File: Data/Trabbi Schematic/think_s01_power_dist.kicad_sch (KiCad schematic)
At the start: 3 parts, among them SW1 Ignition Switch

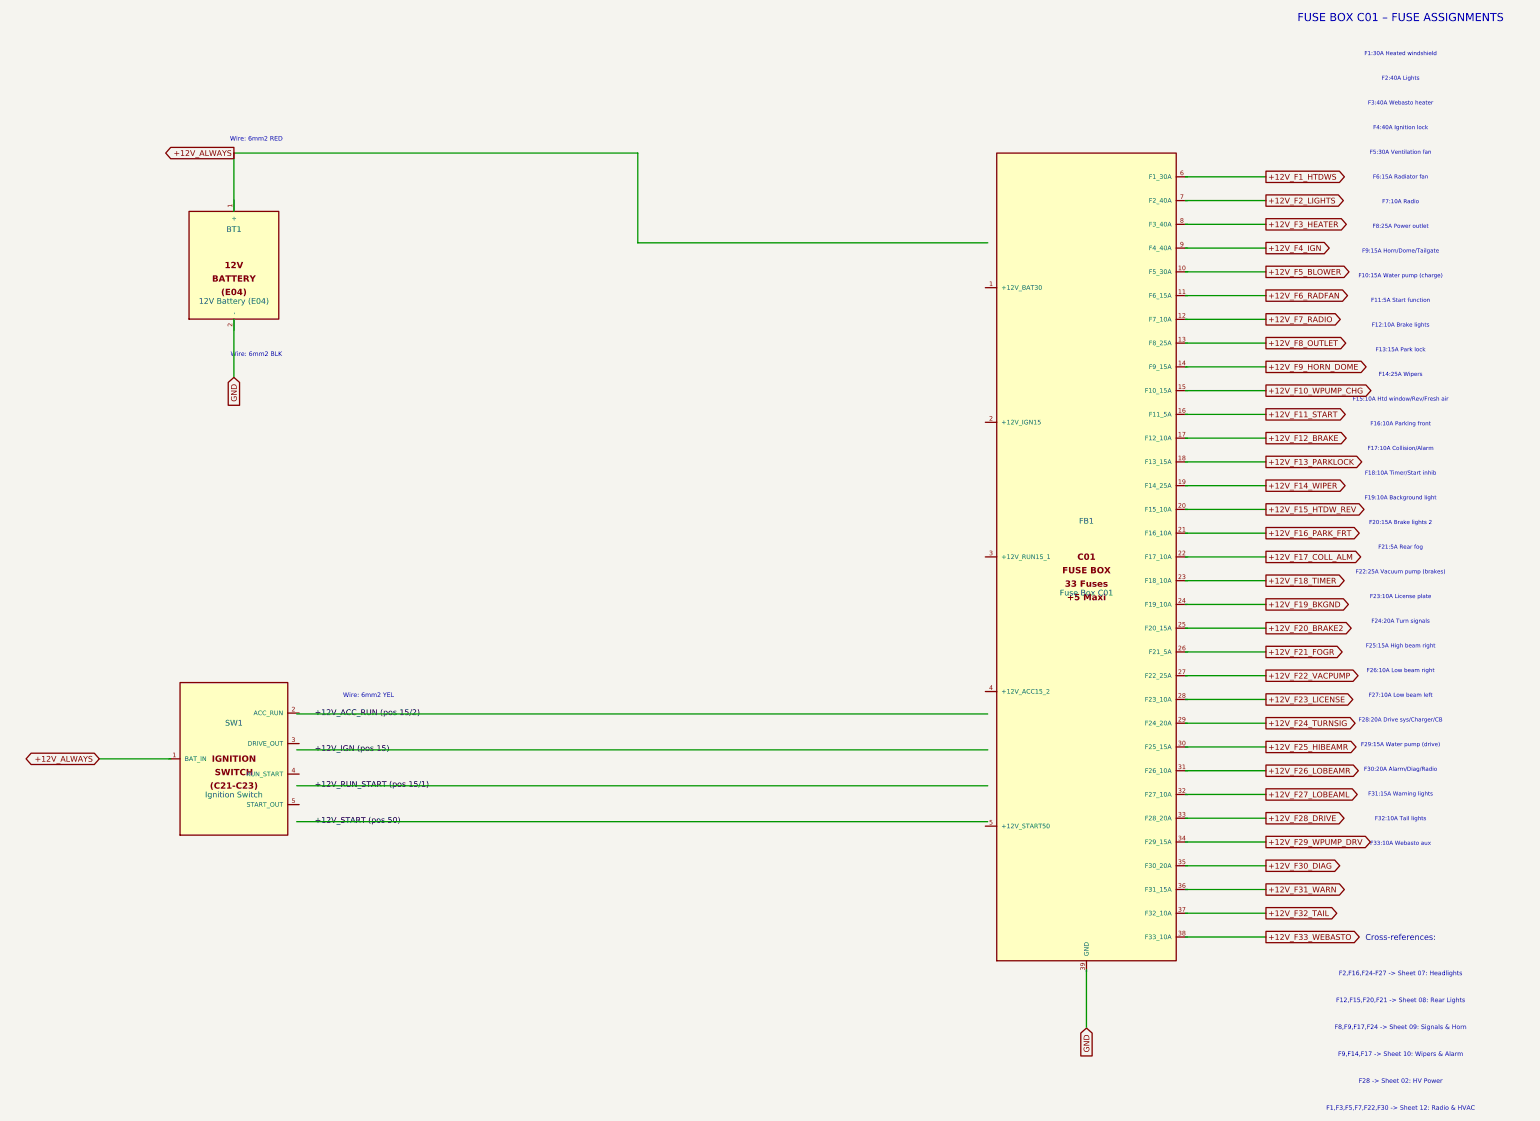
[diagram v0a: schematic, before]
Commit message: Fix wire-to-pin connections: use exact calculated pin positions
Refactored gen_think_complete.py to compute exact pin schematic
coordinates instead of using approximate manual offsets. Added p()
method to Sheet class that transforms symbol-local pin positions to
schematic coordinates. All 232 wire calls across 13 sub-sheet
generators now use p() for pin endpoints, fixing misaligned
connections (previously off by 0.54-10+ units).

Co-Authored-By: Claude Opus 4.6 <noreply@anthropic.com>
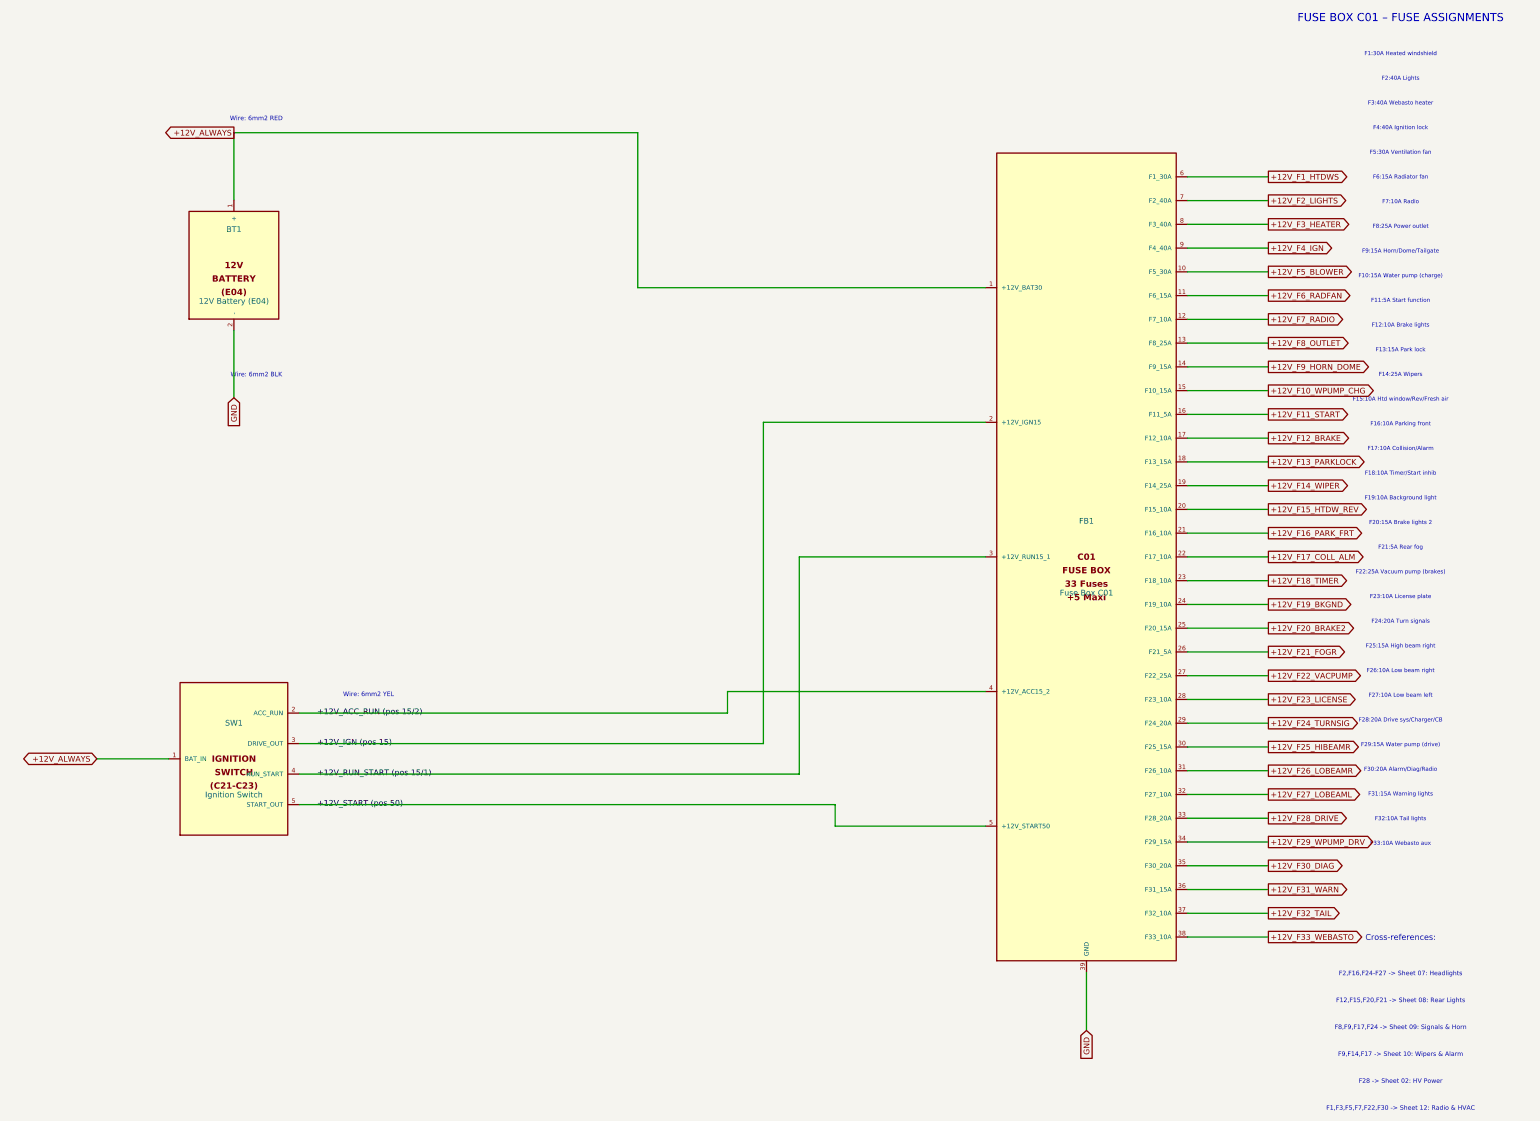
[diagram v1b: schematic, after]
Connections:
- net +12V_ACC_RUN (pos 15/2): now also FB1.4 (+12V_ACC15_2), SW1.2 (ACC_RUN)
- net +12V_ALWAYS: now also BT1.1 (+), FB1.1 (+12V_BAT30), SW1.1 (BAT_IN)
- net +12V_F10_WPUMP_CHG: now also FB1.15 (F10_15A)
- net +12V_F11_START: now also FB1.16 (F11_5A)
- net +12V_F12_BRAKE: now also FB1.17 (F12_10A)
- net +12V_F13_PARKLOCK: now also FB1.18 (F13_15A)
- net +12V_F14_WIPER: now also FB1.19 (F14_25A)
- net +12V_F15_HTDW_REV: now also FB1.20 (F15_10A)
- net +12V_F16_PARK_FRT: now also FB1.21 (F16_10A)
- net +12V_F17_COLL_ALM: now also FB1.22 (F17_10A)
- net +12V_F18_TIMER: now also FB1.23 (F18_10A)
- net +12V_F19_BKGND: now also FB1.24 (F19_10A)
- net +12V_F1_HTDWS: now also FB1.6 (F1_30A)
- net +12V_F20_BRAKE2: now also FB1.25 (F20_15A)
- net +12V_F21_FOGR: now also FB1.26 (F21_5A)
- net +12V_F22_VACPUMP: now also FB1.27 (F22_25A)
- net +12V_F23_LICENSE: now also FB1.28 (F23_10A)
- net +12V_F24_TURNSIG: now also FB1.29 (F24_20A)
- net +12V_F25_HIBEAMR: now also FB1.30 (F25_15A)
- net +12V_F26_LOBEAMR: now also FB1.31 (F26_10A)
- net +12V_F27_LOBEAML: now also FB1.32 (F27_10A)
- net +12V_F28_DRIVE: now also FB1.33 (F28_20A)
- net +12V_F29_WPUMP_DRV: now also FB1.34 (F29_15A)
- net +12V_F2_LIGHTS: now also FB1.7 (F2_40A)
- net +12V_F30_DIAG: now also FB1.35 (F30_20A)
- net +12V_F31_WARN: now also FB1.36 (F31_15A)
- net +12V_F32_TAIL: now also FB1.37 (F32_10A)
- net +12V_F33_WEBASTO: now also FB1.38 (F33_10A)
- net +12V_F3_HEATER: now also FB1.8 (F3_40A)
- net +12V_F4_IGN: now also FB1.9 (F4_40A)
- net +12V_F5_BLOWER: now also FB1.10 (F5_30A)
- net +12V_F6_RADFAN: now also FB1.11 (F6_15A)
- net +12V_F7_RADIO: now also FB1.12 (F7_10A)
- net +12V_F8_OUTLET: now also FB1.13 (F8_25A)
- net +12V_F9_HORN_DOME: now also FB1.14 (F9_15A)
- net +12V_IGN (pos 15): now also FB1.2 (+12V_IGN15), SW1.3 (DRIVE_OUT)
- net +12V_RUN_START (pos 15/1): now also FB1.3 (+12V_RUN15_1), SW1.4 (RUN_START)
- net +12V_START (pos 50): now also FB1.5 (+12V_START50), SW1.5 (START_OUT)
- net GND: now also BT1.2 (-), FB1.39 (GND)

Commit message: Enforce orthogonal routing and 1.27mm grid alignment
- Add _g() grid snap function to Sheet class (rounds all coordinates to nearest 1.27mm)
- Add wire_l() method for L-shaped orthogonal routing (horizontal+vertical segments)
- Apply grid snapping in p(), place(), wire(), label(), glabel(), junction(), no_connect(), defsym()
- Replace all 19 diagonal wire calls with wire_l() across S02, S06, S07, S08, S10, S12, S13
- All wire segments now strictly horizontal or vertical, no diagonals
- All coordinates verified on 1.27mm (50mil) KiCad standard grid

Co-Authored-By: Claude Opus 4.6 <noreply@anthropic.com>
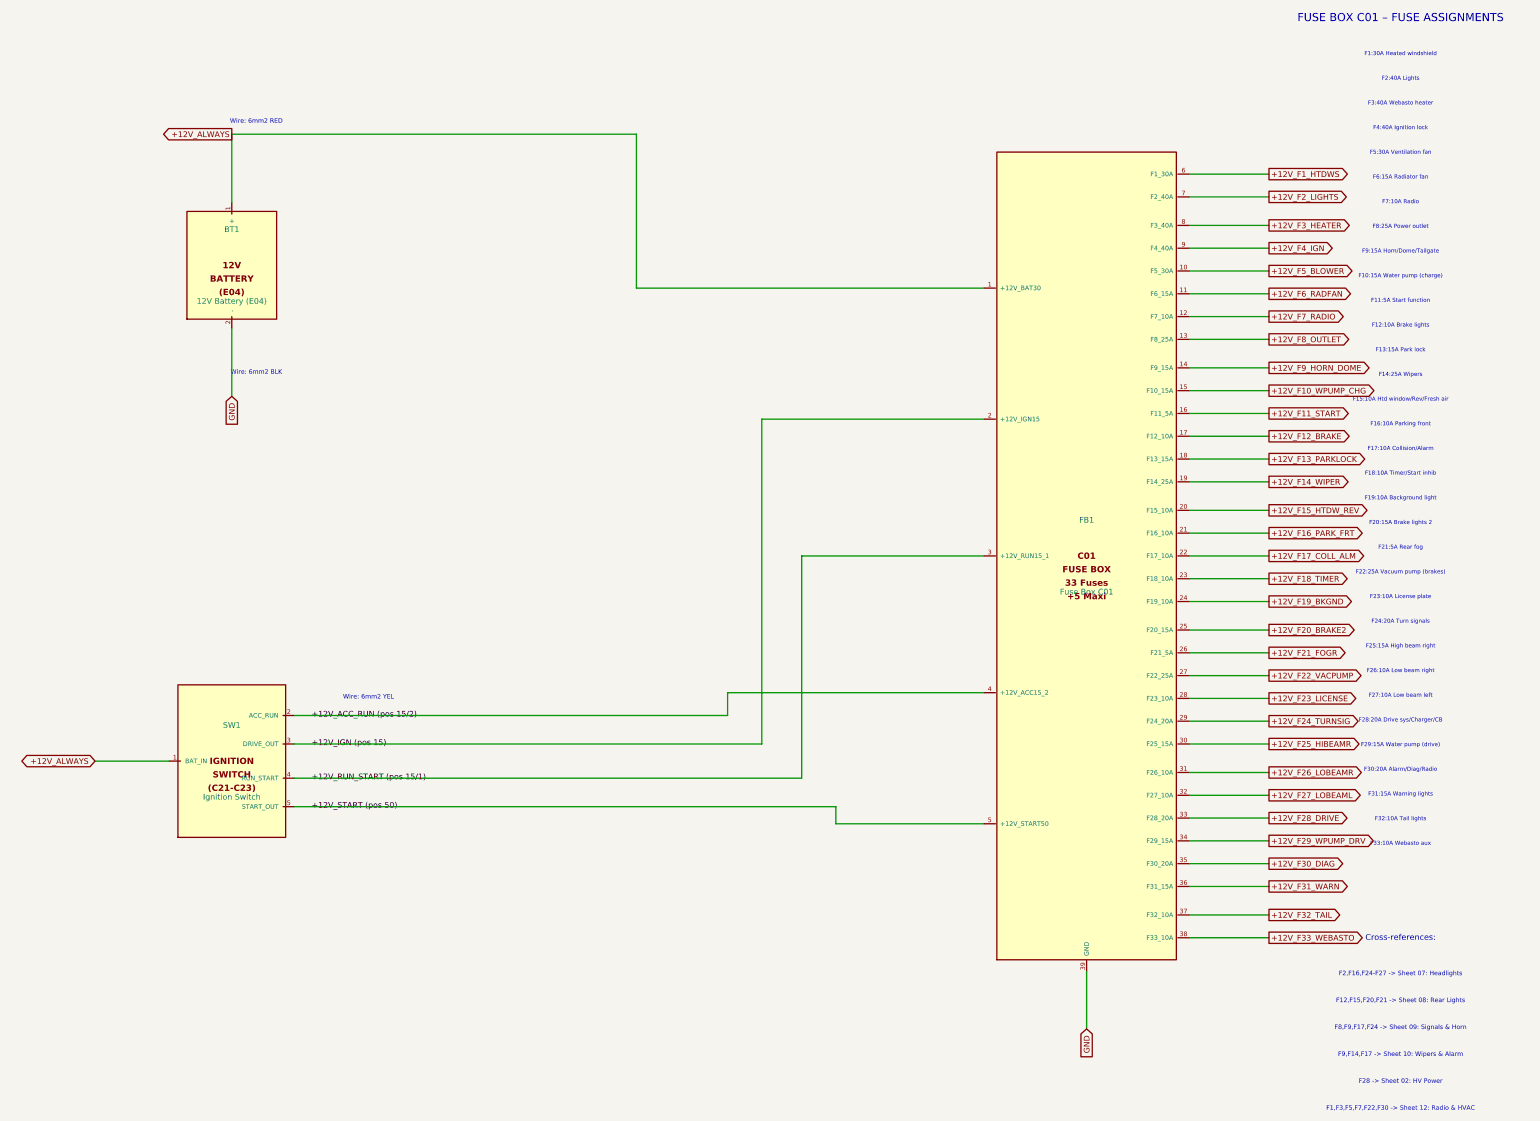
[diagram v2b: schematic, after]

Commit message: Add relay coil/switch graphics, fix label positioning
- Draw coil (inductor arcs) and switch contacts (circles + arm)
  inside RELAY_SPST and RELAY_SPDT symbol bodies
- Add body_gfx parameter to defsym() for custom symbol graphics
- Helper functions: _gfx_polyline, _gfx_arc, _gfx_circle, _relay_gfx
- Fix label offsets: increase from 3-5mm to 10-12mm to avoid
  overlapping pin names (S01 ignition, S02 HV, S05 DCDC, S07 lights)
- Fix S09 turn signal rear labels: add wire stubs (were at 0 offset)
- All 14 schematics regenerated, parentheses balanced, grid OK

Co-Authored-By: Claude Opus 4.6 <noreply@anthropic.com>
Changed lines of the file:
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@@
     (stroke (width 0) (type default))
   )
-  (label "+12V_ACC_RUN (pos 15/2)" (at 67.310 180.340 0)
+  (label "+12V_ACC_RUN (pos 15/2)" (at 73.660 180.340 0)
     (effects (font (size 1.27 1.27)))
   )
@@
     (stroke (width 0) (type default))
   )
-  (label "+12V_IGN (pos 15)" (at 67.310 186.690 0)
+  (label "+12V_IGN (pos 15)" (at 73.660 186.690 0)
     (effects (font (size 1.27 1.27)))
   )
@@
     (stroke (width 0) (type default))
   )
-  (label "+12V_RUN_START (pos 15/1)" (at 67.310 194.310 0)
+  (label "+12V_RUN_START (pos 15/1)" (at 73.660 194.310 0)
     (effects (font (size 1.27 1.27)))
   )
@@
     (stroke (width 0) (type default))
   )
-  (label "+12V_START (pos 50)" (at 67.310 200.660 0)
+  (label "+12V_START (pos 50)" (at 73.660 200.660 0)
     (effects (font (size 1.27 1.27)))
   )
